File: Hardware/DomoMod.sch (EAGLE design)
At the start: 47 parts, among them Q1 BSS138, Q2 BSS138, T1 MMBT2222A, U1 NCS36000, U2 CCS811, U3 BME280, U4 PIR

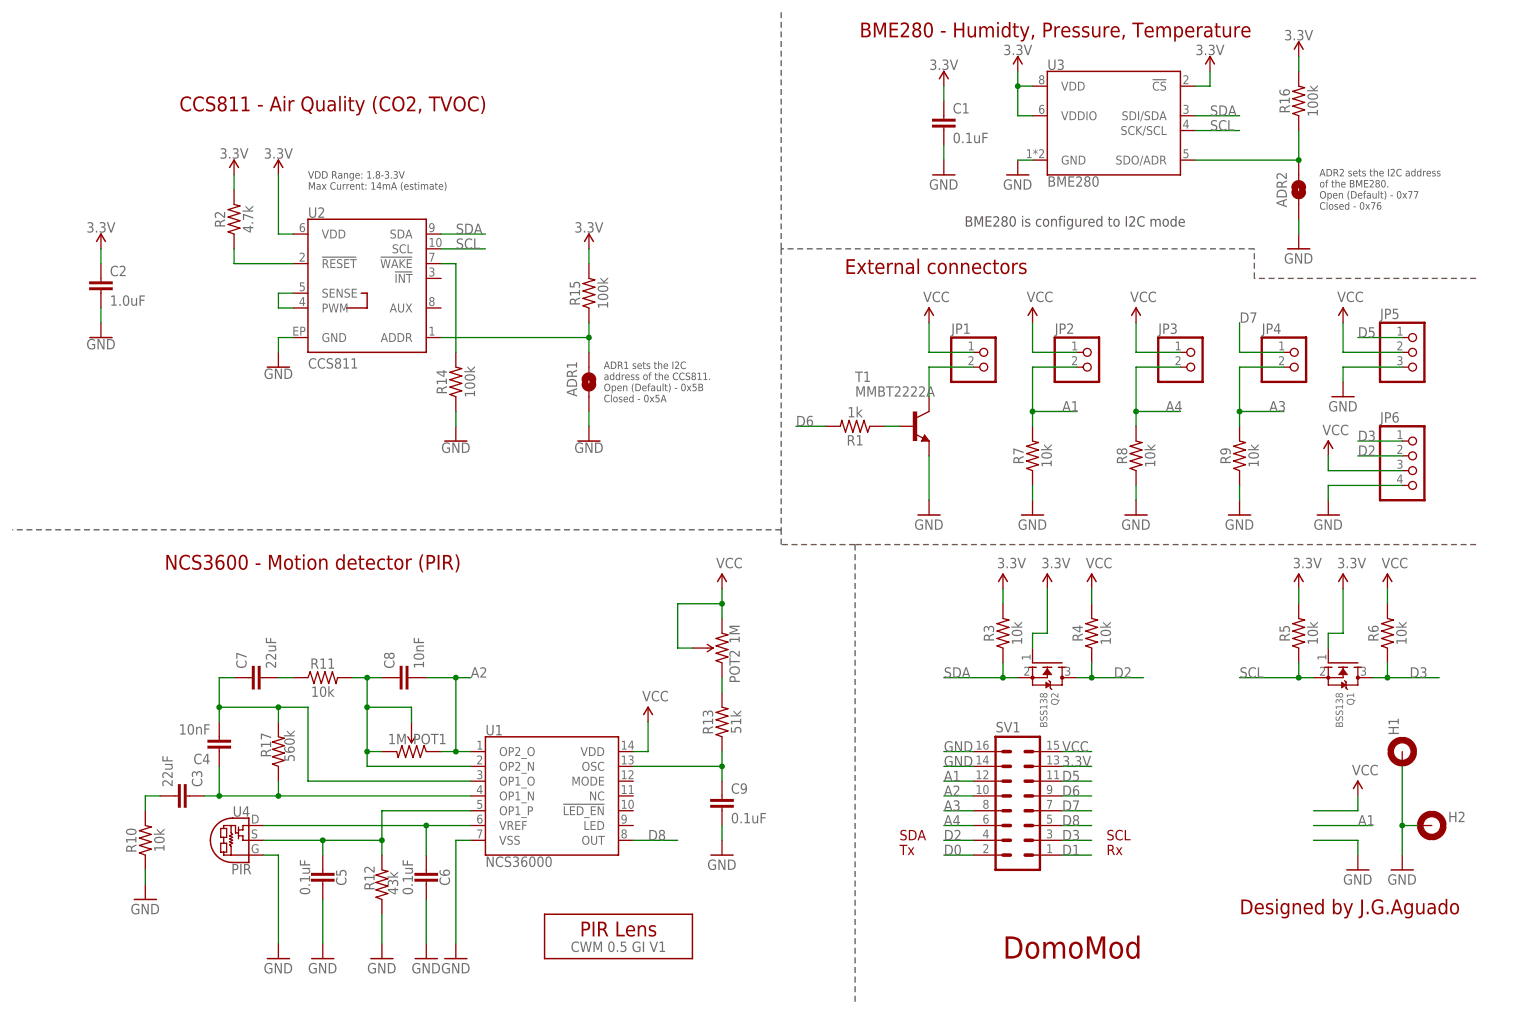
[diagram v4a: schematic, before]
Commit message: Component replacement: NCS36000 -> BD9251FV
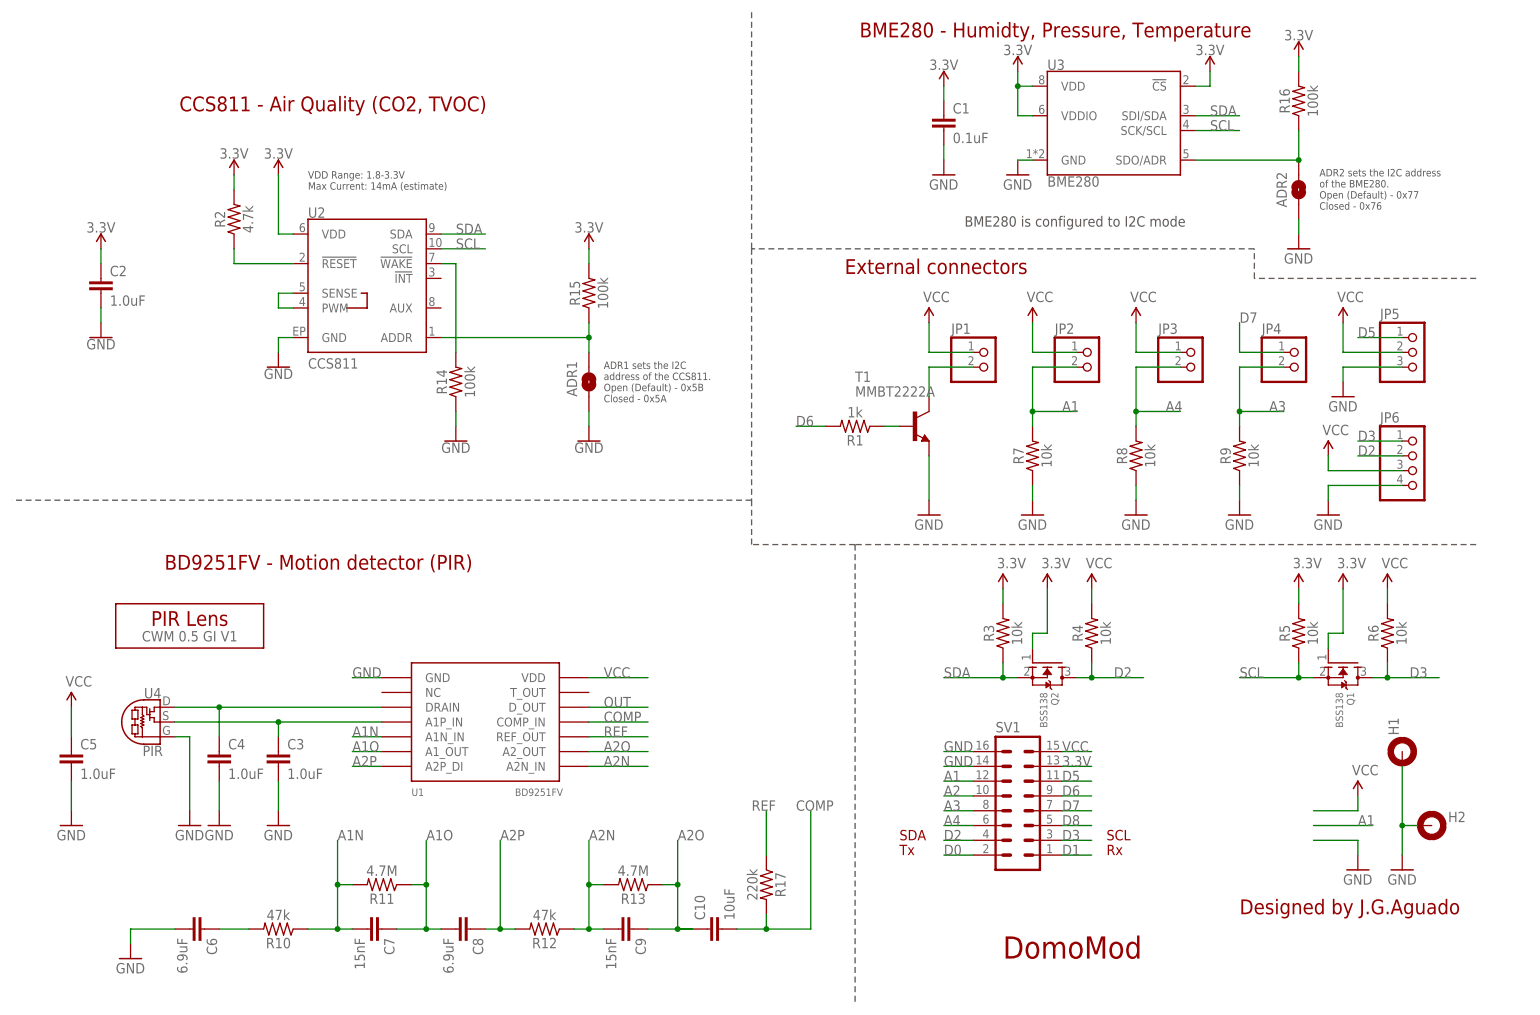
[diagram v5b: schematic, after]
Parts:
- removed POT1, POT2: 1M, openPIR-temp:TRIMPOTTX33X-1M
- added C10: 10uF, SparkFun-Capacitors:1.0UF-0603-16V-10%
- C3: value 22uF -> 1.0uF; device SparkFun-Capacitors:22UF-0805-6.3V-20% -> SparkFun-Capacitors:1.0UF-0603-16V-10%
- C4: value 10nF -> 1.0uF; device SparkFun-Capacitors:10NF-0603-50V-10% -> SparkFun-Capacitors:1.0UF-0603-16V-10%
- C5: value 0.1uF -> 1.0uF; device SparkFun-Capacitors:0.1UF-0603-25V-(+80/-20%) -> SparkFun-Capacitors:1.0UF-0603-16V-10%
- C6: value 0.1uF -> 6.9uF; device SparkFun-Capacitors:0.1UF-0603-25V-(+80/-20%) -> SparkFun-Capacitors:1.0UF-0603-16V-10%
- C7: value 22uF -> 15nF; device SparkFun-Capacitors:22UF-0805-6.3V-20% -> SparkFun-Capacitors:1.0UF-0603-16V-10%
- C8: value 10nF -> 6.9uF; device SparkFun-Capacitors:10NF-0603-50V-10% -> SparkFun-Capacitors:1.0UF-0603-16V-10%
- C9: value 0.1uF -> 15nF; device SparkFun-Capacitors:0.1UF-0603-25V-(+80/-20%) -> SparkFun-Capacitors:1.0UF-0603-16V-10%
- R10: value 10k -> 47k; device SparkFun-Resistors:10KOHM-0603-1/10W-1% -> SparkFun-Resistors:100KOHM-0603-1/10W-1%
- R11: value 10k -> 4.7M; device SparkFun-Resistors:10KOHM-0603-1/10W-1% -> SparkFun-Resistors:100KOHM-0603-1/10W-1%
- R12: value 43k -> 47k; device SparkFun-Resistors:43KOHM-0603-1/10W-1% -> SparkFun-Resistors:100KOHM-0603-1/10W-1%
- R13: value 51k -> 4.7M; device openPIR-temp:51KOHM-0603-1/10W-1% -> SparkFun-Resistors:100KOHM-0603-1/10W-1%
- R17: value 560k -> 220k; device openPIR-temp:560KOHM-0603-1/10W-5% -> SparkFun-Resistors:100KOHM-0603-1/10W-1%
- U1: value NCS36000 -> BD9251FV; device openPIR-temp:NCS36000 -> SpaceDIY_IC:BD9251FV
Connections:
- removed net N$11: POT2.CCW, R13.2
- removed net N$3: C3.2, R10.2
- removed net N$4: C7.2, R11.1
- removed net N$6: C4.2, C7.1, R17.2, U1.OP1_O
- removed net N$7: C8.1, POT1.CW, POT1.WIPER, R11.2, U1.OP2_N
- removed net N$8: C9.1, R13.1, U1.OSC
- new net A1N: C7.2, R10.1, R11.2, U1.A1N_IN
- new net A1O: C7.1, C8.2, R11.1, U1.A1_OUT
- new net A2N: C9.2, R12.1, R13.2, U1.A2N_IN
- new net A2O: C10.1, C9.1, R13.1, U1.A2_OUT
- new net A2P: C8.1, R12.2, U1.A2P_DI
- new net COMP: C10.2, R17.2, U1.COMP_IN
- new net OUT: U1.D_OUT
- new net REF: R17.1, U1.REF_OUT
- net A2: no longer C8.2, POT1.CCW, U1.OP2_O
- net D8: no longer U1.OUT
- net GND: now also C3.2, C4.2, U1.GND; no longer C9.2, R10.1, R12.1, U1.VSS
- net N$1: now also C6.1, R10.2; no longer C5.1, R12.2, U1.OP1_P, U4.S
- net N$2: now also C3.1, U1.A1P_IN, U4.S; no longer C6.1, U1.VREF, U4.D
- net N$5: now also U1.DRAIN, U4.D; no longer C3.1, R17.1, U1.OP1_N
- net VCC: now also C5.1; no longer POT2.CW, POT2.WIPER
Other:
- note added: "BD9251FV - Motion detector (PIR)"
- note removed: "NCS3600 - Motion detector (PIR)"
- moved on the sheet: C3, C4, C5, C6, C7, C8, C9, R10, R11, R12, R13, R17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

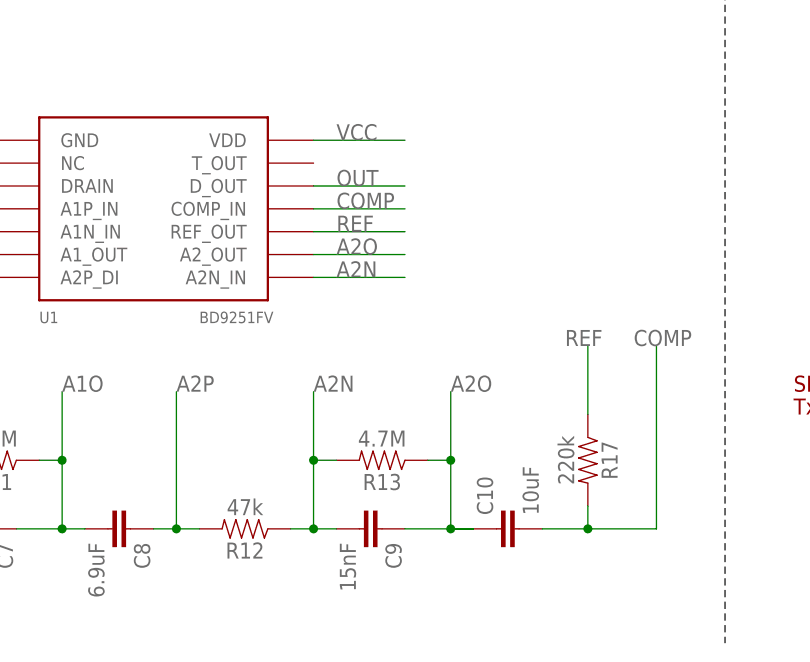
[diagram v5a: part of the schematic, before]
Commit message: BRD and Production files updated for component BD9251FV
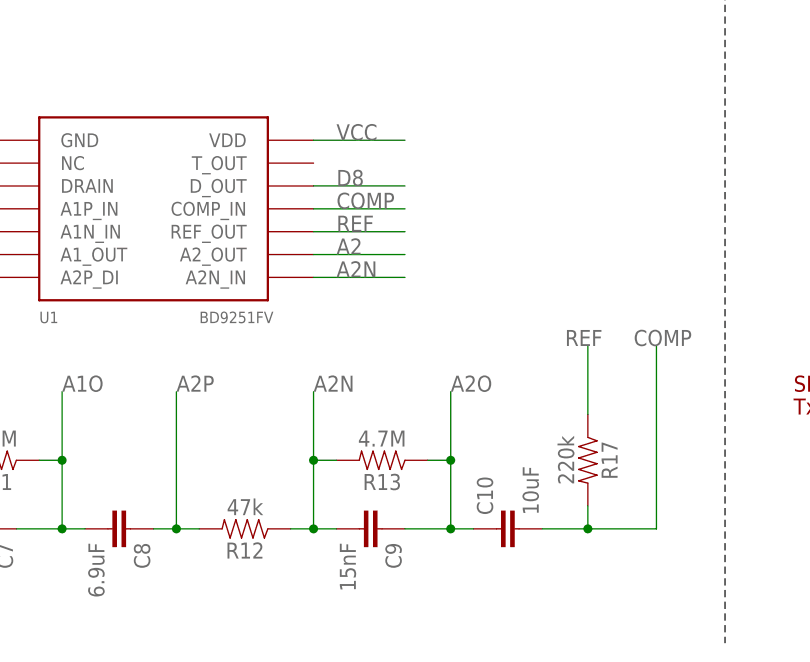
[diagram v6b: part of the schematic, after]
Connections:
- removed net OUT: U1.D_OUT
- net A2: now also U1.A2_OUT
- net A2O: no longer U1.A2_OUT
- net D8: now also U1.D_OUT
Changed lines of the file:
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@@
 <pinref part="SV1" gate="G$1" pin="10"/>
+</segment>
+<segment>
+<pinref part="U1" gate="G$1" pin="A2_OUT"/>
+<wire x1="114.3" y1="48.26" x2="104.14" y2="48.26" width="0.1524" layer="91"/>
+<label x="106.68" y="48.26" size="1.778" layer="95"/>
 </segment>
 </net>
@@
 <label x="185.42" y="35.56" size="1.778" layer="95"/>
 <pinref part="SV1" gate="G$1" pin="5"/>
+</segment>
+<segment>
+<pinref part="U1" gate="G$1" pin="D_OUT"/>
+<wire x1="104.14" y1="55.88" x2="114.3" y2="55.88" width="0.1524" layer="91"/>
+<label x="106.68" y="55.88" size="1.778" layer="95"/>
 </segment>
 </net>
@@
 <net name="A2O" class="0">
 <segment>
-<pinref part="U1" gate="G$1" pin="A2_OUT"/>
-<wire x1="114.3" y1="48.26" x2="104.14" y2="48.26" width="0.1524" layer="91"/>
-<label x="106.68" y="48.26" size="1.778" layer="95"/>
-</segment>
-<segment>
 <pinref part="C9" gate="G$1" pin="1"/>
 <pinref part="C10" gate="G$1" pin="1"/>
 <wire x1="114.3" y1="17.78" x2="119.38" y2="17.78" width="0.1524" layer="91"/>
-<wire x1="119.38" y1="17.78" x2="121.92" y2="17.78" width="0.1524" layer="91"/>
 <wire x1="121.92" y1="17.78" x2="119.38" y2="17.78" width="0.1524" layer="91"/>
 <wire x1="119.38" y1="17.78" x2="119.38" y2="25.4" width="0.1524" layer="91"/>
@@
 </segment>
 </net>
-<net name="OUT" class="0">
-<segment>
-<pinref part="U1" gate="G$1" pin="D_OUT"/>
-<wire x1="104.14" y1="55.88" x2="114.3" y2="55.88" width="0.1524" layer="91"/>
-<label x="106.68" y="55.88" size="1.778" layer="95"/>
-</segment>
-</net>

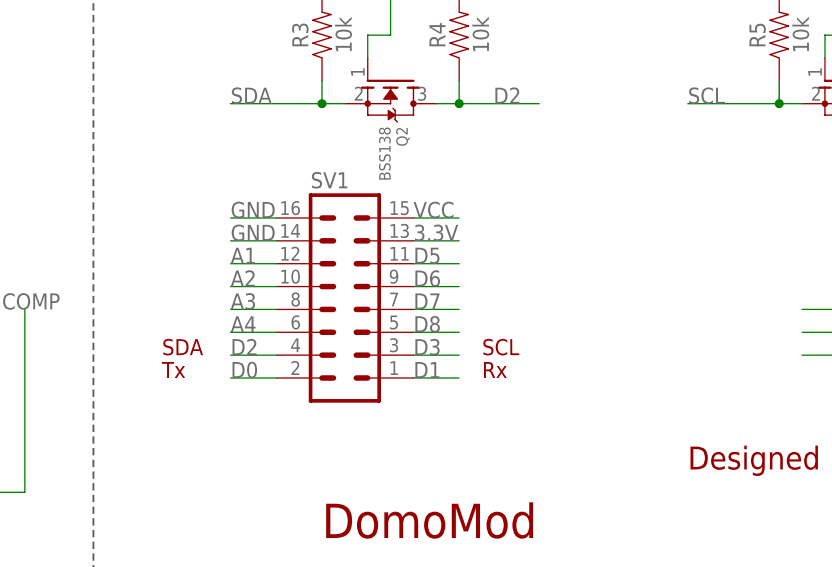
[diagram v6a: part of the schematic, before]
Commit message: Fixed connector interface (rows were changed)
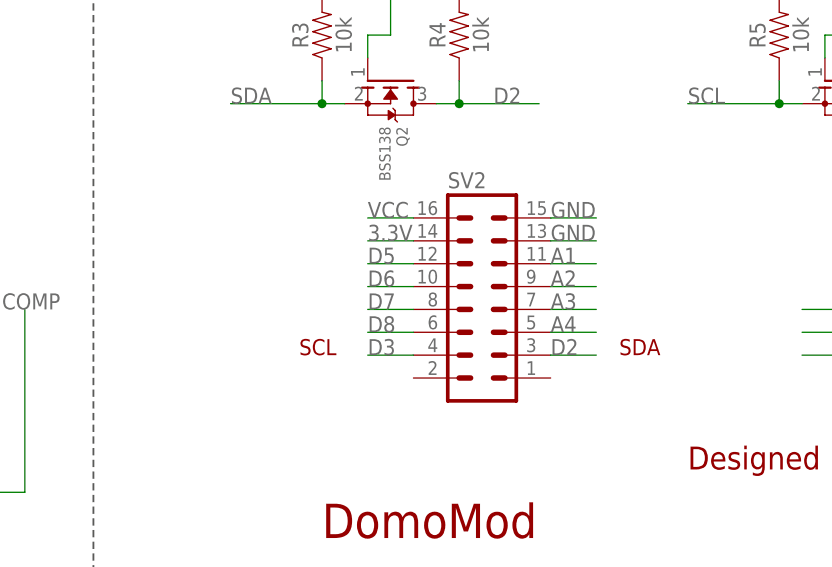
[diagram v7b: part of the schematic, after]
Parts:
- removed SV1: (no value), con-lstb:MA08-2
- added SV2: (no value), con-lstb:MA08-2
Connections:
- removed net D0: SV1.2
- removed net D1: SV1.1
- net 3.3V: now also SV2.14; no longer SV1.13
- net A1: now also SV2.11; no longer SV1.12
- net A2: now also SV2.9; no longer SV1.10
- net A3: now also SV2.7; no longer SV1.8
- net A4: now also SV2.5; no longer SV1.6
- net D2: now also SV2.3; no longer SV1.4
- net D3: now also SV2.4; no longer SV1.3
- net D5: now also SV2.12; no longer SV1.11
- net D6: now also SV2.10; no longer SV1.9
- net D7: now also SV2.8; no longer SV1.7
- net D8: now also SV2.6; no longer SV1.5
- net GND: now also SV2.13, SV2.15; no longer SV1.14, SV1.16
- net VCC: now also SV2.16; no longer SV1.15
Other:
- note removed: "Rx"
- note removed: "Tx"

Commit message: Updated design files
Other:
- note added: "LDR"
- note added: "MOISTURE"
- note added: "NTC"
- moved on the sheet: JP1, JP2, JP3, JP4, JP5, JP6, R1, R7, R8, R9, T1
